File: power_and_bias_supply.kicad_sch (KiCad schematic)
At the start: 44 parts, among them Q501 2N7002, U501 MCP6L02x-xSN, X5 Conn_Coaxial

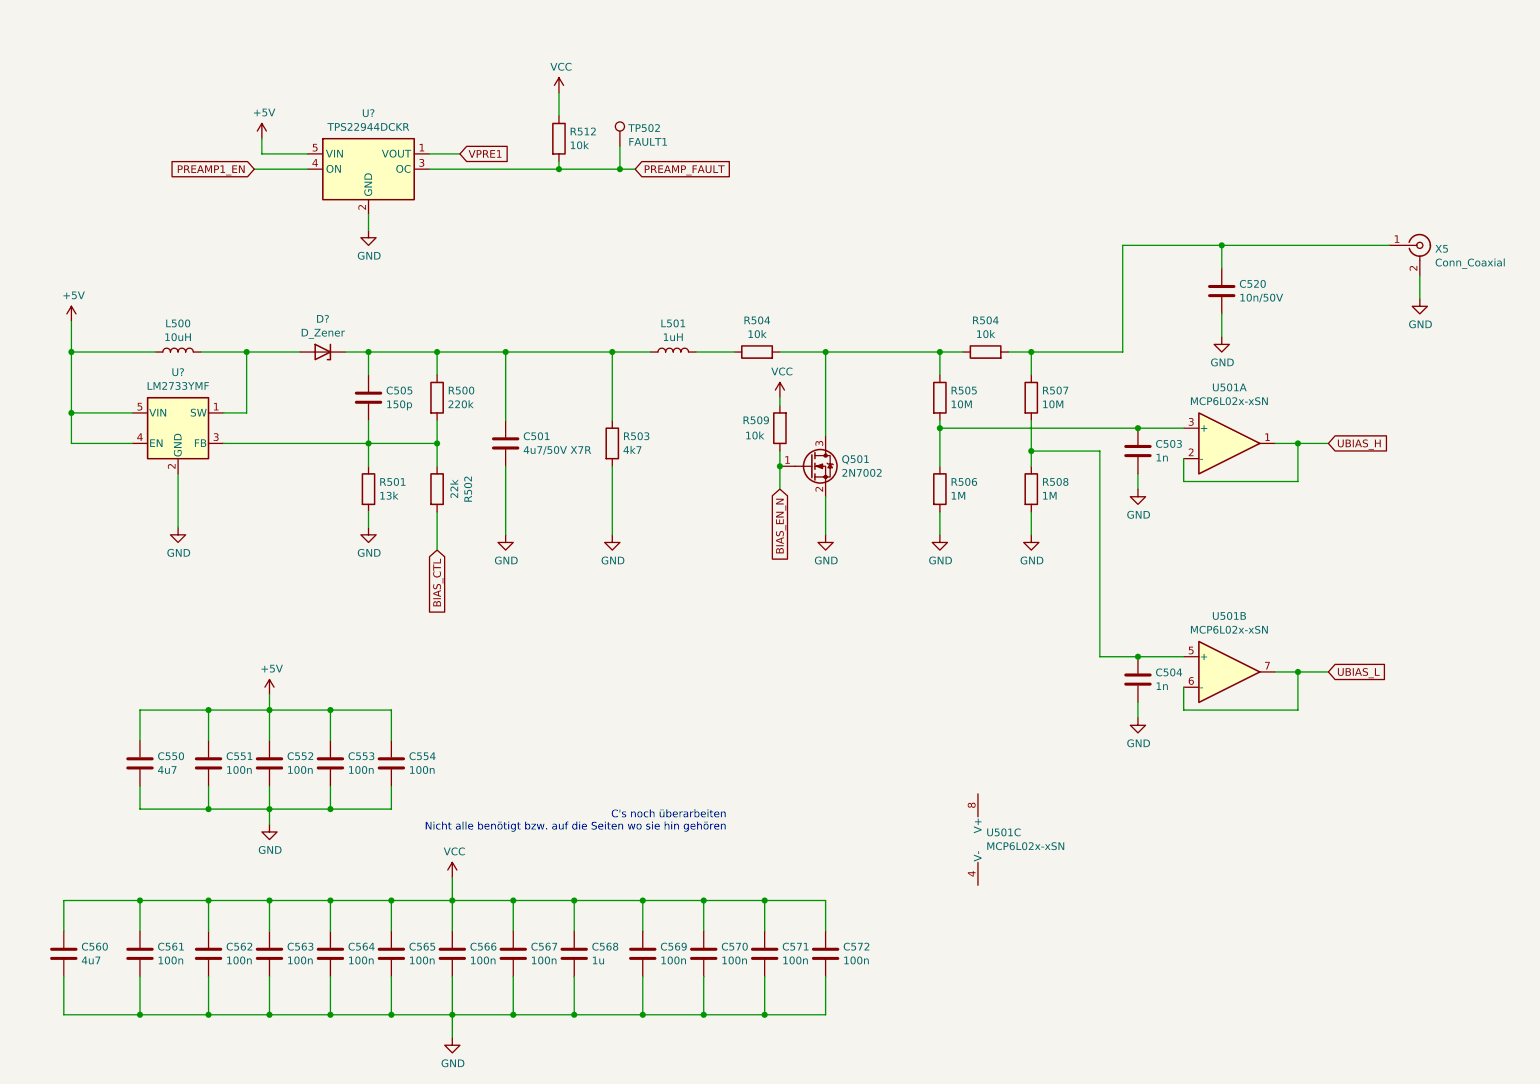
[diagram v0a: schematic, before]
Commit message: Changes in BOM. Add JLCpcb Part Nr
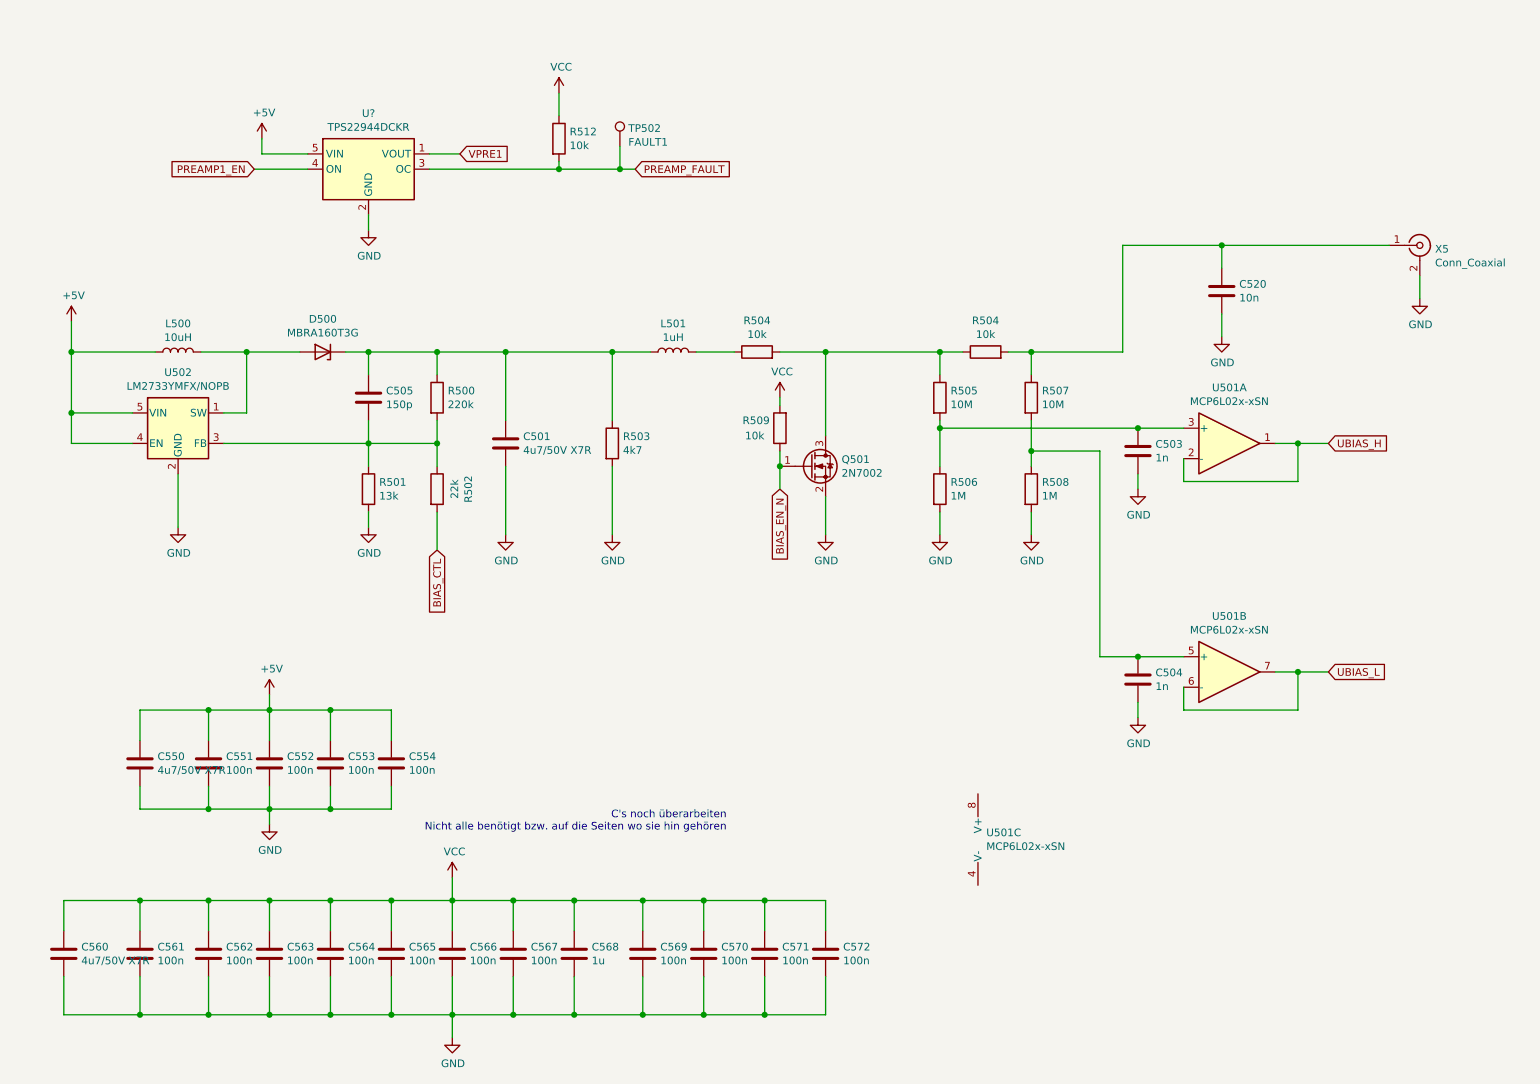
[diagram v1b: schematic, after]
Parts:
- C501: footprint (none) -> Capacitor_SMD:C_1206_3216Metric_Pad1.33x1.80mm_HandSolder; JLCBasicPart (none) -> Basic; JLCPartNr (none) -> C29823; JLCType (none) -> 1206B475K500NT; OriginalType (none) -> GRM31CR71H475KA12L
- C503, C504: footprint (none) -> Capacitor_SMD:C_0805_2012Metric_Pad1.18x1.45mm_HandSolder; JLCBasicPart (none) -> Basic; JLCPartNr (none) -> C46653; JLCType (none) -> CL21B102KBCNNNC; OriginalType (none) -> 0805B102K500CT
- C505: footprint (none) -> Capacitor_SMD:C_0805_2012Metric_Pad1.18x1.45mm_HandSolder; JLCBasicPart (none) -> Basic; JLCPartNr (none) -> C1716; JLCType (none) -> 0805B151K500NT; OriginalType (none) -> TCC0805X7R151K500BT
- C520: value 10n/50V -> 10n; footprint (none) -> Capacitor_SMD:C_0805_2012Metric_Pad1.18x1.45mm_HandSolder; JLCBasicPart (none) -> Basic; JLCPartNr (none) -> C1710; JLCType (none) -> CL21B103KBANNNC; OriginalType (none) -> GRM216R71H103KA01D
- C550, C560: value 4u7 -> 4u7/50V X7R; footprint (none) -> Capacitor_SMD:C_1206_3216Metric_Pad1.33x1.80mm_HandSolder; JLCBasicPart (none) -> Basic; JLCPartNr (none) -> C29823; JLCType (none) -> 1206B475K500NT; OriginalType (none) -> GRM31CR71H475KA12L
- C551, C552, C553, C554, C561, C562, C563, C564, C565, C566, C567, C569, C570, C571, C572: footprint (none) -> Capacitor_SMD:C_0805_2012Metric_Pad1.18x1.45mm_HandSolder; JLCBasicPart (none) -> Basic; JLCPartNr (none) -> C49678; JLCType (none) -> CC0805KRX7R9BB104; OriginalType (none) -> FN21X104K500PXG
- C568: footprint (none) -> Capacitor_SMD:C_0805_2012Metric_Pad1.18x1.45mm_HandSolder; JLCBasicPart (none) -> Basic; JLCPartNr (none) -> C28323; JLCType (none) -> CL21B105KBFNNNE; OriginalType (none) -> CL21B105KBFNNNE
- D500: renamed from D?; value D_Zener -> MBRA160T3G; footprint (none) -> Diode_SMD:D_SMA; JLCBasicPart (none) -> Extended; JLCPartNr (none) -> C49187; JLCType (none) -> MBRA160T3G; OriginalType (none) -> MBRA160T3G
- L500: footprint (none) -> Inductor_SMD:L_1812_4532Metric_Pad1.30x3.40mm_HandSolder; OriginalType (none) -> LQH43MN100J03L; Supplier (none) -> LCSC
- L501: footprint (none) -> Inductor_SMD:L_0805_2012Metric_Pad1.15x1.40mm_HandSolder; OriginalType (none) -> L-15F1R0JV4E; Supplier (none) -> Mouser
- R500: footprint (none) -> Resistor_SMD:R_0805_2012Metric_Pad1.20x1.40mm_HandSolder; JLCBasicPart (none) -> Basic; JLCPartNr (none) -> C17556; JLCType (none) -> 0805W8F2203T5E; OriginalType (none) -> RS-05K224JT
- R501: footprint (none) -> Resistor_SMD:R_0805_2012Metric_Pad1.20x1.40mm_HandSolder; JLCBasicPart (none) -> Basic; JLCPartNr (none) -> C17455; JLCType (none) -> 0805W8F1302T5E; OriginalType (none) -> 0805W8F1302T5E
- R502: footprint (none) -> Resistor_SMD:R_0805_2012Metric_Pad1.20x1.40mm_HandSolder; JLCBasicPart (none) -> Basic; JLCPartNr (none) -> C17560; JLCType (none) -> 0805W8F2202T5E; OriginalType (none) -> 0805W8F2202T5E
- R503: footprint (none) -> Resistor_SMD:R_0805_2012Metric_Pad1.20x1.40mm_HandSolder; JLCBasicPart (none) -> Basic; JLCPartNr (none) -> C17673; JLCType (none) -> 0805W8F4701T5E; OriginalType (none) -> RK73B2ATTD472J
- R504, R509, R512: footprint (none) -> Resistor_SMD:R_0805_2012Metric_Pad1.20x1.40mm_HandSolder; JLCBasicPart (none) -> Basic; JLCPartNr (none) -> C17414; JLCType (none) -> 0805W8F1002T5E; OriginalType (none) -> WR08X1002FTL
- R505, R507: footprint (none) -> Resistor_SMD:R_0805_2012Metric_Pad1.20x1.40mm_HandSolder; JLCBasicPart (none) -> Basic; JLCPartNr (none) -> C26108; JLCType (none) -> 0805W8F1005T5E; OriginalType (none) -> RTT051005FTP
- R506, R508: footprint (none) -> Resistor_SMD:R_0805_2012Metric_Pad1.20x1.40mm_HandSolder; JLCBasicPart (none) -> Basic; JLCPartNr (none) -> C17514; JLCType (none) -> 0805W8F1004T5E; OriginalType (none) -> RS-05K1004FT
- U502: renamed from U?; value LM2733YMF -> LM2733YMFX/NOPB; JLCBasicPart (none) -> Extended; JLCPartNr (none) -> C527399; JLCType (none) -> LM2733YMFX/NOPB; OriginalType (none) -> LM2733YMFX/NOPB; Supplier (none) -> LCSC

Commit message: Minor Fixes
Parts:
- renumbered R504 to R516
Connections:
- net GND: now also U501.4 (V-)
- net VCC: now also U501.8 (V+)
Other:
- moved on the sheet: U501C
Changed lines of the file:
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@@
+    (stroke (width 0) (type solid) (color 0 0 0 0))
+  )
+  (wire (pts (xy 177.8 135.89) (xy 177.8 137.16))
+    (stroke (width 0) (type solid) (color 0 0 0 0))
+  )
+  (wire (pts (xy 177.8 152.4) (xy 177.8 154.94))
     (stroke (width 0) (type solid) (color 0 0 0 0))
   )
@@
     (pin "1")
   )
+  (symbol (lib_id "power:VCC") (at 177.8 135.89 0) (unit 1)
+    (in_bom yes) (on_board yes)
+    (property "Reference" "#PWR0195" (id 0) (at 177.8 139.7 0)
+      (effects (font (size 1.27 1.27)) hide)
+    )
+    (property "Value" "VCC" (id 1) (at 178.1683 131.5656 0))
+    (property "Footprint" "" (id 2) (at 177.8 135.89 0)
+      (effects (font (size 1.27 1.27)) hide)
+    )
+    (property "Datasheet" "" (id 3) (at 177.8 135.89 0)
+      (effects (font (size 1.27 1.27)) hide)
+    )
+    (pin "1")
+  )
   (symbol (lib_id "Connector:TestPoint") (at 120.65 38.1 0) (unit 1)
     (in_bom yes) (on_board yes)
@@
     )
     (property "Datasheet" "" (id 3) (at 173.99 102.87 0)
+      (effects (font (size 1.27 1.27)) hide)
+    )
+    (pin "1")
+  )
+  (symbol (lib_id "power:GND") (at 177.8 154.94 0) (unit 1)
+    (in_bom yes) (on_board yes)
+    (property "Reference" "#PWR0194" (id 0) (at 177.8 161.29 0)
+      (effects (font (size 1.27 1.27)) hide)
+    )
+    (property "Value" "GND" (id 1) (at 177.9143 159.2644 0))
+    (property "Footprint" "" (id 2) (at 177.8 154.94 0)
+      (effects (font (size 1.27 1.27)) hide)
+    )
+    (property "Datasheet" "" (id 3) (at 177.8 154.94 0)
       (effects (font (size 1.27 1.27)) hide)
     )
@@
     (pin "2")
   )
-  (symbol (lib_id "Amplifier_Operational:MCP6L02x-xSN") (at 180.34 153.67 0) (unit 3)
-    (in_bom yes) (on_board yes)
-    (property "Reference" "U501" (id 0) (at 181.7244 152.5206 0)
-      (effects (font (size 1.27 1.27)) (justify left))
-    )
-    (property "Value" "MCP6L02x-xSN" (id 1) (at 181.7244 154.8193 0)
-      (effects (font (size 1.27 1.27)) (justify left))
-    )
-    (property "Footprint" "Package_SO:SOIC-8_3.9x4.9mm_P1.27mm" (id 2) (at 182.88 153.67 0)
-      (effects (font (size 1.27 1.27)) hide)
-    )
-    (property "Datasheet" "http://ww1.microchip.com/downloads/en/devicedoc/22140b.pdf" (id 3) (at 186.69 149.86 0)
+  (symbol (lib_id "Amplifier_Operational:MCP6L02x-xSN") (at 177.8 144.78 0) (unit 3)
+    (in_bom yes) (on_board yes)
+    (property "Reference" "U501" (id 0) (at 179.1844 143.6306 0)
+      (effects (font (size 1.27 1.27)) (justify left))
+    )
+    (property "Value" "MCP6L02x-xSN" (id 1) (at 179.1844 145.9293 0)
+      (effects (font (size 1.27 1.27)) (justify left))
+    )
+    (property "Footprint" "Package_SO:SOIC-8_3.9x4.9mm_P1.27mm" (id 2) (at 180.34 144.78 0)
+      (effects (font (size 1.27 1.27)) hide)
+    )
+    (property "Datasheet" "http://ww1.microchip.com/downloads/en/devicedoc/22140b.pdf" (id 3) (at 184.15 140.97 0)
       (effects (font (size 1.27 1.27)) hide)
     )
@@
   (symbol (lib_id "Device:R") (at 143.51 72.39 90) (unit 1)
     (in_bom yes) (on_board yes)
-    (property "Reference" "R504" (id 0) (at 143.51 67.1638 90))
+    (property "Reference" "R516" (id 0) (at 143.51 67.1638 90))
     (property "Value" "10k" (id 1) (at 143.51 69.4625 90))
     (property "Footprint" "Resistor_SMD:R_0805_2012Metric_Pad1.20x1.40mm_HandSolder" (id 2) (at 143.51 74.168 90)

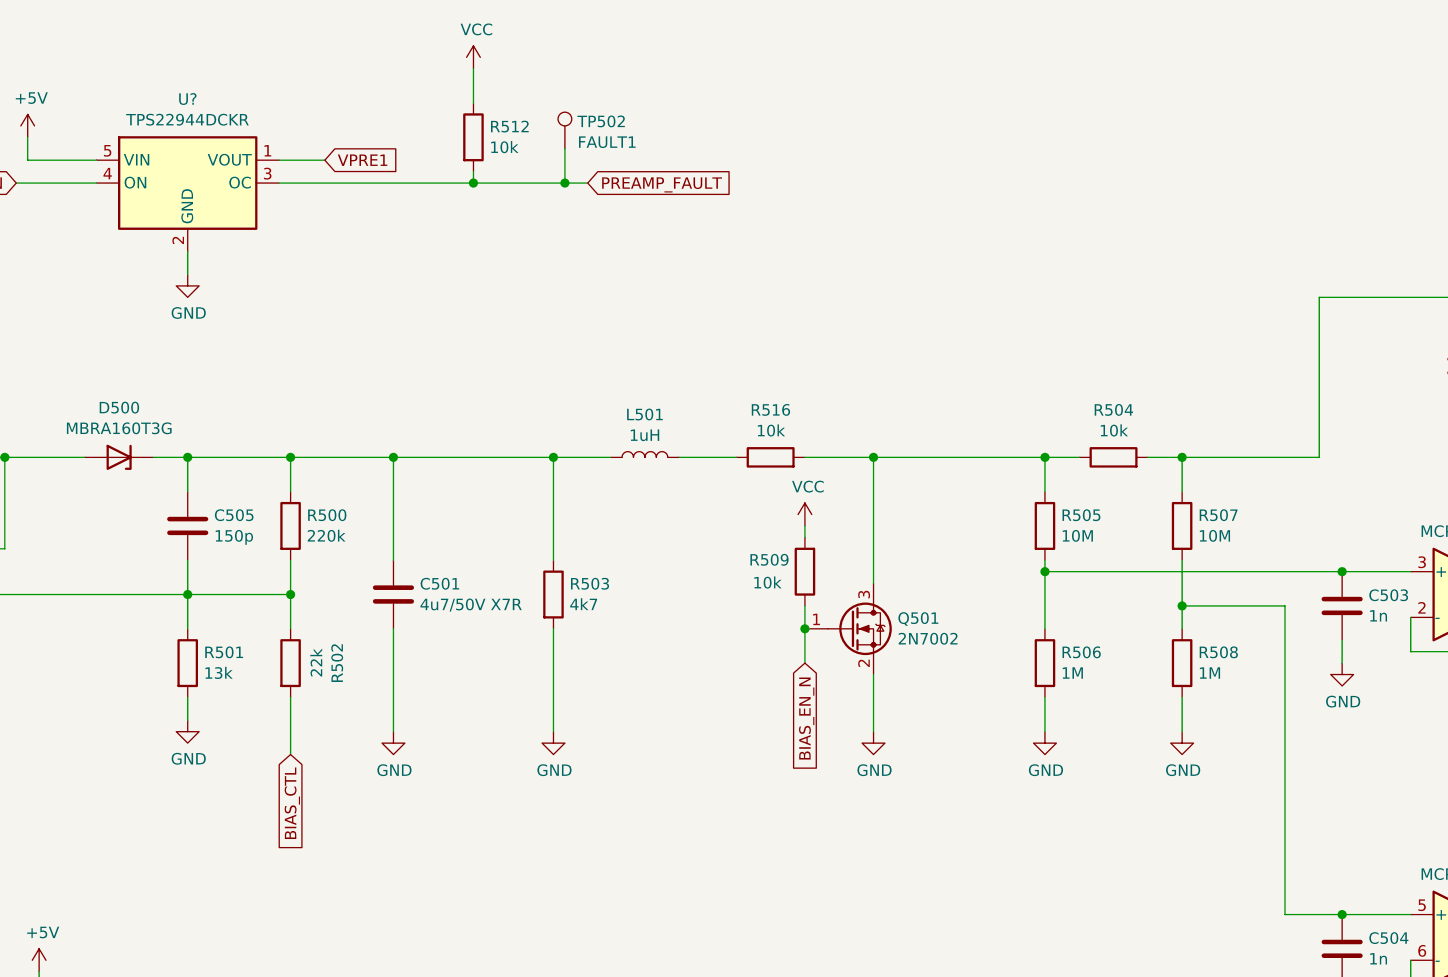
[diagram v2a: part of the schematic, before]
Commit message: working on BOM. Small Fixes in Schematics
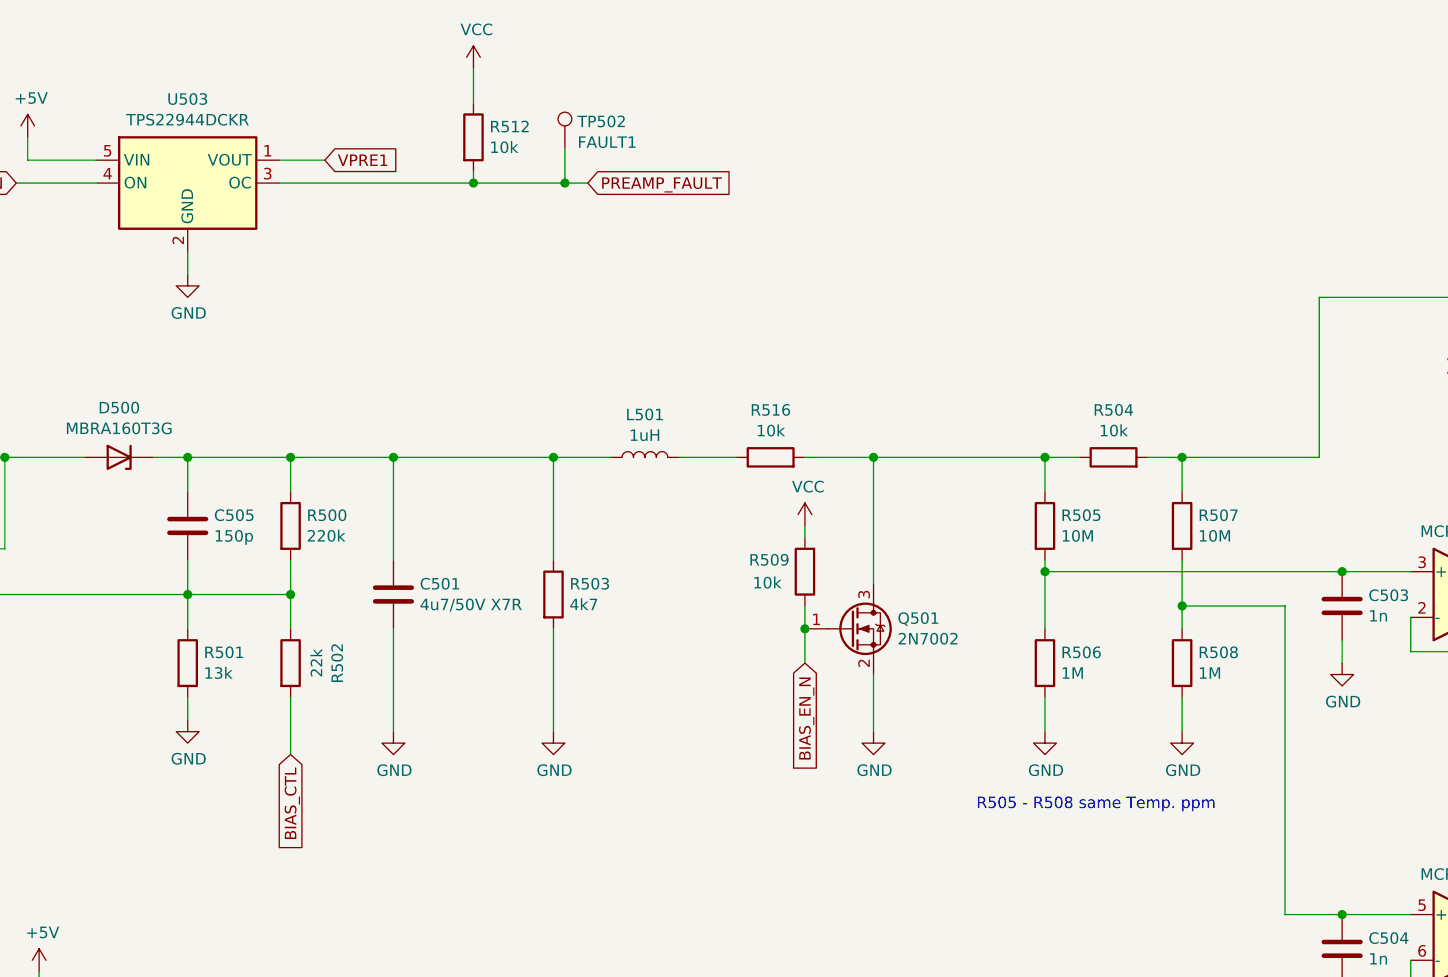
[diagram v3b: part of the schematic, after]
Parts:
- Q501: JLCBasicPart (none) -> Basic; JLCPartNr (none) -> C8545; JLCType (none) -> 2N7002; OriginalType (none) -> C8545; Supplier (none) -> LCSC
- gave numbers to parts that had none: 1
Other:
- note added: "R505 - R508 same Temp. ppm"
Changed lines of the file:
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@@
     (effects (font (size 1.27 1.27)) (justify right bottom))
+  )
+  (text "R505 - R508 same Temp. ppm" (at 166.37 111.76 0)
+    (effects (font (size 1.27 1.27)) (justify left bottom))
   )
   (global_label "PREAMP1_EN" (shape input) (at 59.69 41.91 180)
@@
       (effects (font (size 1.27 1.27) italic) (justify left) hide)
     )
-    (property "Datasheet" "https://www.onsemi.com/pub/Collateral/NDS7002A-D.PDF" (id 3) (at 152.4 91.44 0)
+    (property "Datasheet" "~" (id 3) (at 152.4 91.44 0)
       (effects (font (size 1.27 1.27)) (justify left) hide)
+    )
+    (property "JLCBasicPart" "Basic" (id 4) (at 152.4 91.44 0)
+      (effects (font (size 1.27 1.27)) hide)
+    )
+    (property "JLCPartNr" "C8545" (id 5) (at 152.4 91.44 0)
+      (effects (font (size 1.27 1.27)) hide)
+    )
+    (property "JLCType" "2N7002" (id 6) (at 152.4 91.44 0)
+      (effects (font (size 1.27 1.27)) hide)
+    )
+    (property "OriginalType" "C8545" (id 7) (at 152.4 91.44 0)
+      (effects (font (size 1.27 1.27)) hide)
+    )
+    (property "Supplier" "LCSC" (id 8) (at 152.4 91.44 0)
+      (effects (font (size 1.27 1.27)) hide)
     )
     (pin "1")
@@
   (symbol (lib_id "muonpi-kicad-library:TPS22944DCKR") (at 78.74 41.91 0) (unit 1)
     (in_bom yes) (on_board yes)
-    (property "Reference" "U?" (id 0) (at 78.74 32.6198 0))
+    (property "Reference" "U503" (id 0) (at 78.74 32.6198 0))
     (property "Value" "TPS22944DCKR" (id 1) (at 78.74 34.9185 0))
     (property "Footprint" "" (id 2) (at 78.74 29.21 0)
